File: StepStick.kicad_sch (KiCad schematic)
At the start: 6 parts, among them J1501 Conn_01x08_Female, J1502 Screw_Terminal_01x04, J1503 Conn_02x03_Odd_Even, J1504 Conn_01x08_Female

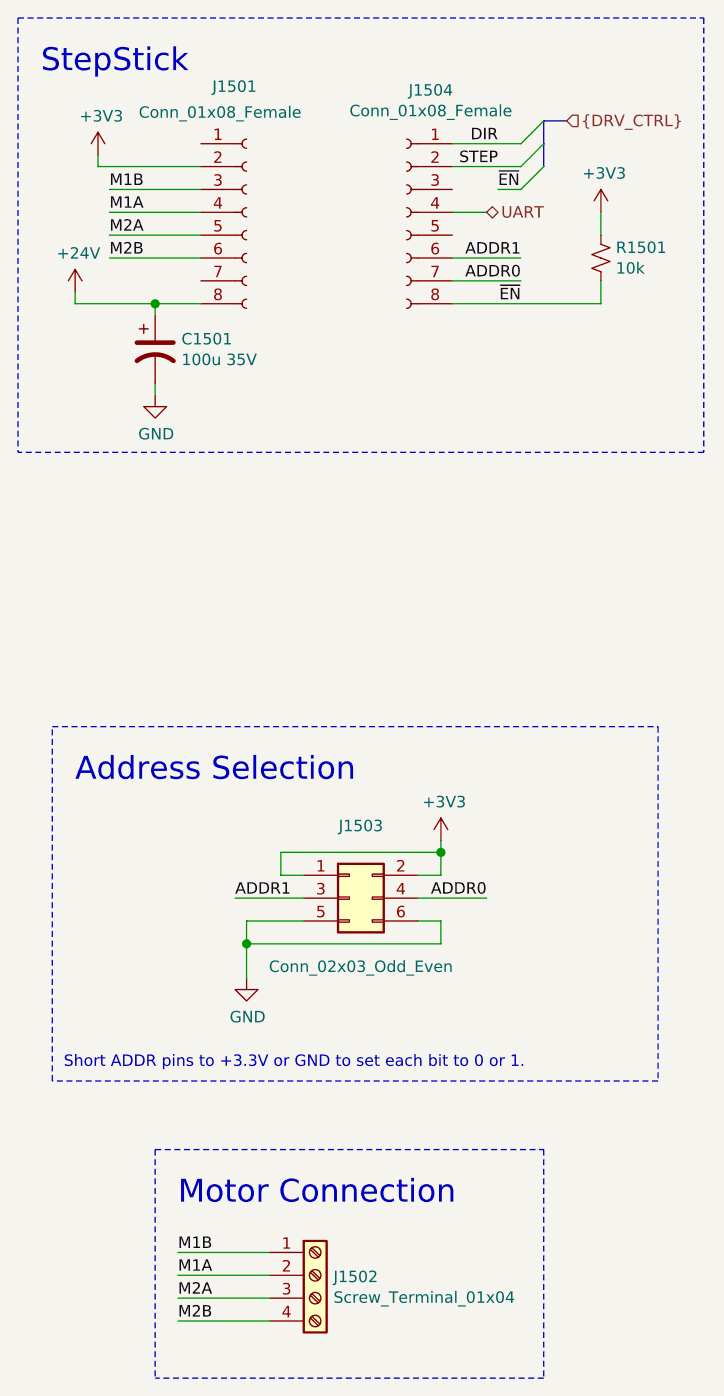
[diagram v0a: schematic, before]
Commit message: Setup git filters h/t https://jnavila.github.io/plotkicadsch/
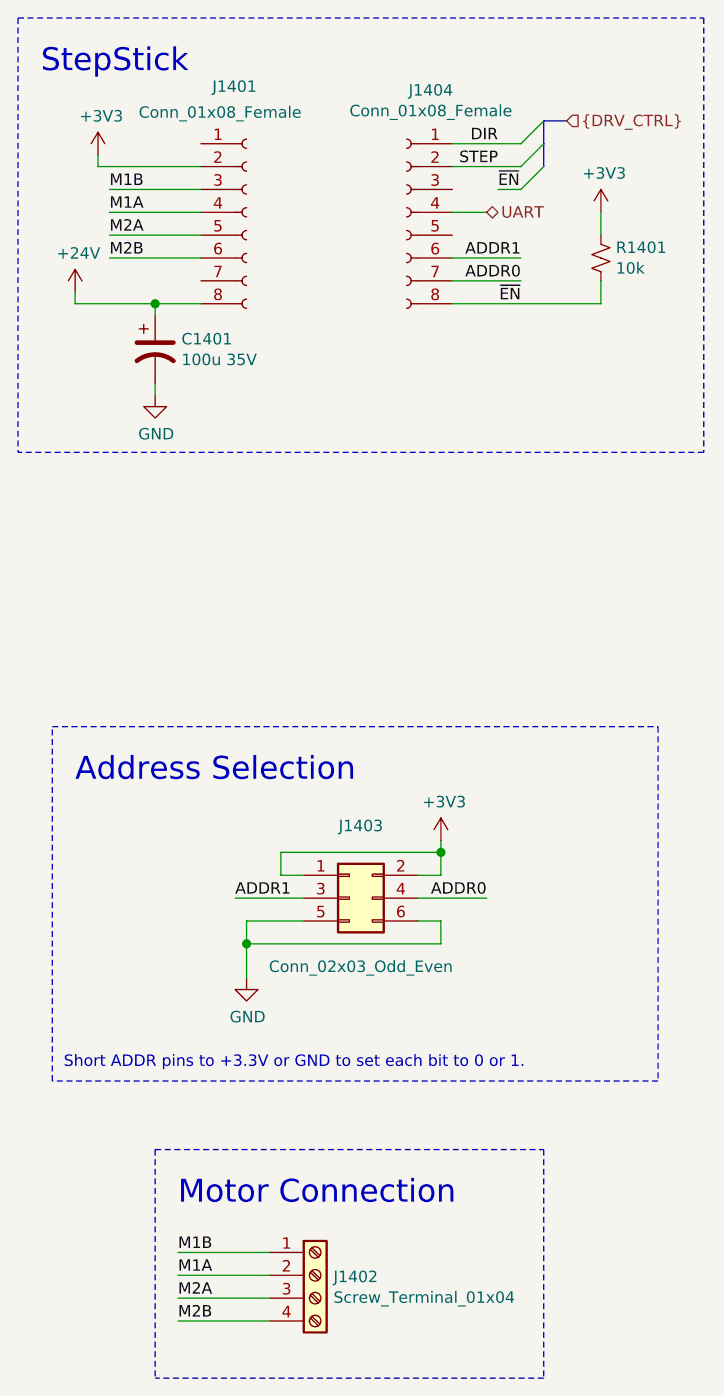
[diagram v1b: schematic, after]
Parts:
- renumbered C1501 to C1401, J1501 to J1401, J1502 to J1402, J1503 to J1403, J1504 to J1404, R1501 to R1401
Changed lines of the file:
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@@
   (symbol (lib_id "power:+24V") (at 180.34 95.25 0)
     (in_bom yes) (on_board yes)
-    (property "Reference" "#PWR01501" (id 0) (at 180.34 99.06 0)
+    (property "Reference" "#PWR?" (id 0) (at 180.34 99.06 0)
       (effects (font (size 1.27 1.27)) hide)
     )
@@
   (symbol (lib_id "power:+3V3") (at 182.88 80.01 0)
     (in_bom yes) (on_board yes)
-    (property "Reference" "#PWR01502" (id 0) (at 182.88 83.82 0)
+    (property "Reference" "#PWR?" (id 0) (at 182.88 83.82 0)
       (effects (font (size 1.27 1.27)) hide)
     )
@@
   (symbol (lib_id "power:+3V3") (at 220.98 156.21 0)
     (in_bom yes) (on_board yes)
-    (property "Reference" "#PWR01505" (id 0) (at 220.98 160.02 0)
+    (property "Reference" "#PWR?" (id 0) (at 220.98 160.02 0)
       (effects (font (size 1.27 1.27)) hide)
     )
@@
   (symbol (lib_id "power:+3V3") (at 238.76 86.36 0)
     (in_bom yes) (on_board yes)
-    (property "Reference" "#PWR01506" (id 0) (at 238.76 90.17 0)
+    (property "Reference" "#PWR?" (id 0) (at 238.76 90.17 0)
       (effects (font (size 1.27 1.27)) hide)
     )
@@
   (symbol (lib_id "power:GND") (at 189.23 106.68 0)
     (in_bom yes) (on_board yes)
-    (property "Reference" "#PWR01503" (id 0) (at 189.23 113.03 0)
+    (property "Reference" "#PWR?" (id 0) (at 189.23 113.03 0)
       (effects (font (size 1.27 1.27)) hide)
     )
@@
   (symbol (lib_id "power:GND") (at 199.39 171.45 0)
     (in_bom yes) (on_board yes)
-    (property "Reference" "#PWR0129" (id 0) (at 199.39 177.8 0)
+    (property "Reference" "#PWR?" (id 0) (at 199.39 177.8 0)
       (effects (font (size 1.27 1.27)) hide)
     )
@@
   (symbol (lib_id "Device:R_Small_US") (at 238.76 91.44 0)
     (in_bom yes) (on_board yes)
-    (property "Reference" "R1501" (id 0) (at 240.4111 90.2906 0)
+    (property "Reference" "R1401" (id 0) (at 240.4111 90.2906 0)
       (effects (font (size 1.27 1.27)) (justify left))
     )
@@
   (symbol (lib_id "Device:CP1") (at 189.23 101.6 0)
     (in_bom yes) (on_board yes)
-    (property "Reference" "C1501" (id 0) (at 192.1511 100.4506 0)
+    (property "Reference" "C1401" (id 0) (at 192.1511 100.4506 0)
       (effects (font (size 1.27 1.27)) (justify left))
     )
@@
   (symbol (lib_id "Connector:Screw_Terminal_01x04") (at 207.01 204.47 0)
     (in_bom yes) (on_board yes)
-    (property "Reference" "J1502" (id 0) (at 209.0421 204.6414 0)
+    (property "Reference" "J1402" (id 0) (at 209.0421 204.6414 0)
       (effects (font (size 1.27 1.27)) (justify left))
     )
@@
   (symbol (lib_id "Connector_Generic:Conn_02x03_Odd_Even") (at 210.82 162.56 0)
     (in_bom yes) (on_board yes)
-    (property "Reference" "J1503" (id 0) (at 212.09 154.5398 0))
+    (property "Reference" "J1403" (id 0) (at 212.09 154.5398 0))
     (property "Value" "Conn_02x03_Odd_Even" (id 1) (at 212.09 170.18 0))
     (property "Footprint" "Connector_PinHeader_2.54mm:PinHeader_2x03_P2.54mm_Vertical" (id 2) (at 210.82 162.56 0)
@@
   (symbol (lib_id "Connector:Conn_01x08_Female") (at 199.39 86.36 0)
     (in_bom yes) (on_board yes)
-    (property "Reference" "J1501" (id 0) (at 195.58 72.39 0)
+    (property "Reference" "J1401" (id 0) (at 195.58 72.39 0)
       (effects (font (size 1.27 1.27)) (justify left))
     )
@@
   (symbol (lib_id "Connector:Conn_01x08_Female") (at 217.17 86.36 0) (mirror y)
     (in_bom yes) (on_board yes)
-    (property "Reference" "J1504" (id 0) (at 219.8624 72.8026 0))
+    (property "Reference" "J1404" (id 0) (at 219.8624 72.8026 0))
     (property "Value" "Conn_01x08_Female" (id 1) (at 219.8624 75.1013 0))
     (property "Footprint" "Connector_PinSocket_2.54mm:PinSocket_1x08_P2.54mm_Vertical" (id 2) (at 217.17 86.36 0)

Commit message: Switch to stacked USB ports
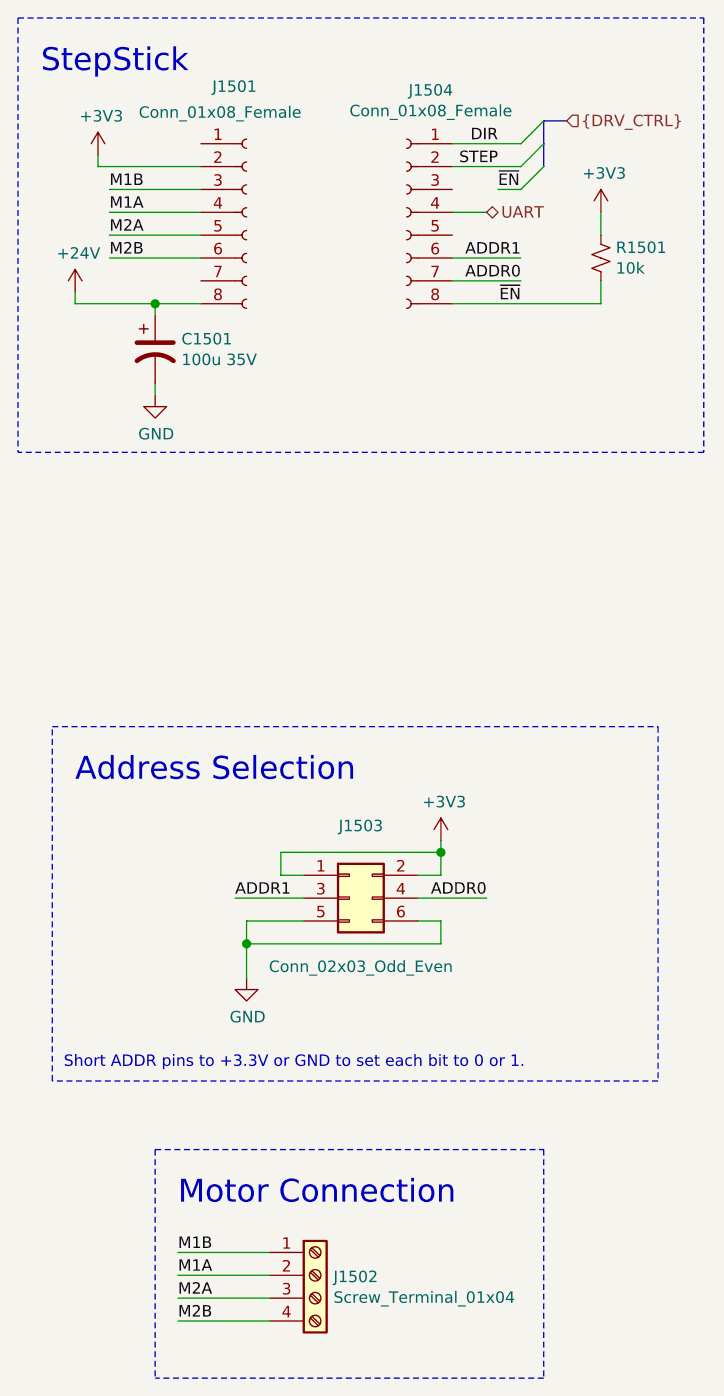
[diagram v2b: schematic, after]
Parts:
- renumbered C1401 to C1501, J1401 to J1501, J1402 to J1502, J1403 to J1503, J1404 to J1504, R1401 to R1501
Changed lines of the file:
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@@
   (symbol (lib_id "Device:R_Small_US") (at 238.76 91.44 0)
     (in_bom yes) (on_board yes)
-    (property "Reference" "R1401" (id 0) (at 240.4111 90.2906 0)
+    (property "Reference" "R1501" (id 0) (at 240.4111 90.2906 0)
       (effects (font (size 1.27 1.27)) (justify left))
     )
@@
   (symbol (lib_id "Device:CP1") (at 189.23 101.6 0)
     (in_bom yes) (on_board yes)
-    (property "Reference" "C1401" (id 0) (at 192.1511 100.4506 0)
+    (property "Reference" "C1501" (id 0) (at 192.1511 100.4506 0)
       (effects (font (size 1.27 1.27)) (justify left))
     )
@@
   (symbol (lib_id "Connector:Screw_Terminal_01x04") (at 207.01 204.47 0)
     (in_bom yes) (on_board yes)
-    (property "Reference" "J1402" (id 0) (at 209.0421 204.6414 0)
+    (property "Reference" "J1502" (id 0) (at 209.0421 204.6414 0)
       (effects (font (size 1.27 1.27)) (justify left))
     )
@@
   (symbol (lib_id "Connector_Generic:Conn_02x03_Odd_Even") (at 210.82 162.56 0)
     (in_bom yes) (on_board yes)
-    (property "Reference" "J1403" (id 0) (at 212.09 154.5398 0))
+    (property "Reference" "J1503" (id 0) (at 212.09 154.5398 0))
     (property "Value" "Conn_02x03_Odd_Even" (id 1) (at 212.09 170.18 0))
     (property "Footprint" "Connector_PinHeader_2.54mm:PinHeader_2x03_P2.54mm_Vertical" (id 2) (at 210.82 162.56 0)
@@
   (symbol (lib_id "Connector:Conn_01x08_Female") (at 199.39 86.36 0)
     (in_bom yes) (on_board yes)
-    (property "Reference" "J1401" (id 0) (at 195.58 72.39 0)
+    (property "Reference" "J1501" (id 0) (at 195.58 72.39 0)
       (effects (font (size 1.27 1.27)) (justify left))
     )
@@
   (symbol (lib_id "Connector:Conn_01x08_Female") (at 217.17 86.36 0) (mirror y)
     (in_bom yes) (on_board yes)
-    (property "Reference" "J1404" (id 0) (at 219.8624 72.8026 0))
+    (property "Reference" "J1504" (id 0) (at 219.8624 72.8026 0))
     (property "Value" "Conn_01x08_Female" (id 1) (at 219.8624 75.1013 0))
     (property "Footprint" "Connector_PinSocket_2.54mm:PinSocket_1x08_P2.54mm_Vertical" (id 2) (at 217.17 86.36 0)

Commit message: Route ULPI signals
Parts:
- R1501: footprint Resistor_SMD:R_0603_1608Metric -> Resistor_SMD:R_0402_1005Metric
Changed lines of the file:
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@@
       (effects (font (size 1.27 1.27)) (justify left))
     )
-    (property "Footprint" "Resistor_SMD:R_0603_1608Metric" (id 2) (at 238.76 91.44 0)
+    (property "Footprint" "Resistor_SMD:R_0402_1005Metric" (id 2) (at 238.76 91.44 0)
       (effects (font (size 1.27 1.27)) hide)
     )
